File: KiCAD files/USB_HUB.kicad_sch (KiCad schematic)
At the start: 23 parts, among them U1 SL2.1S

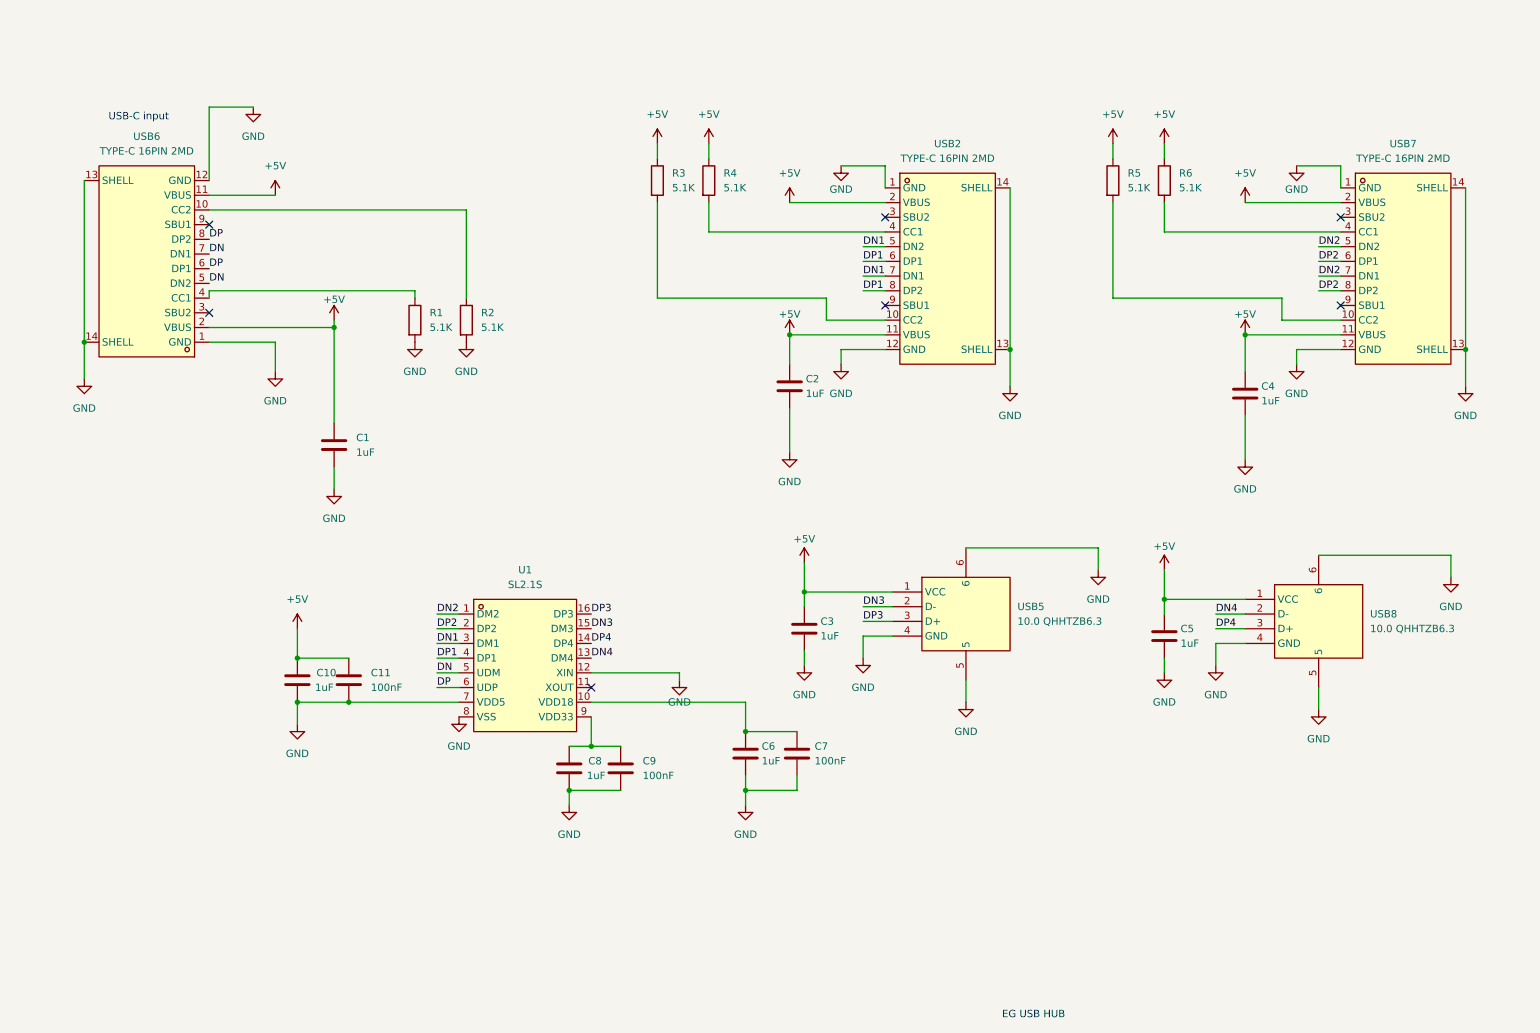
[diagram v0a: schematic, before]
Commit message: Updated board design to include ESD. Not changed: Zine, README except BOM
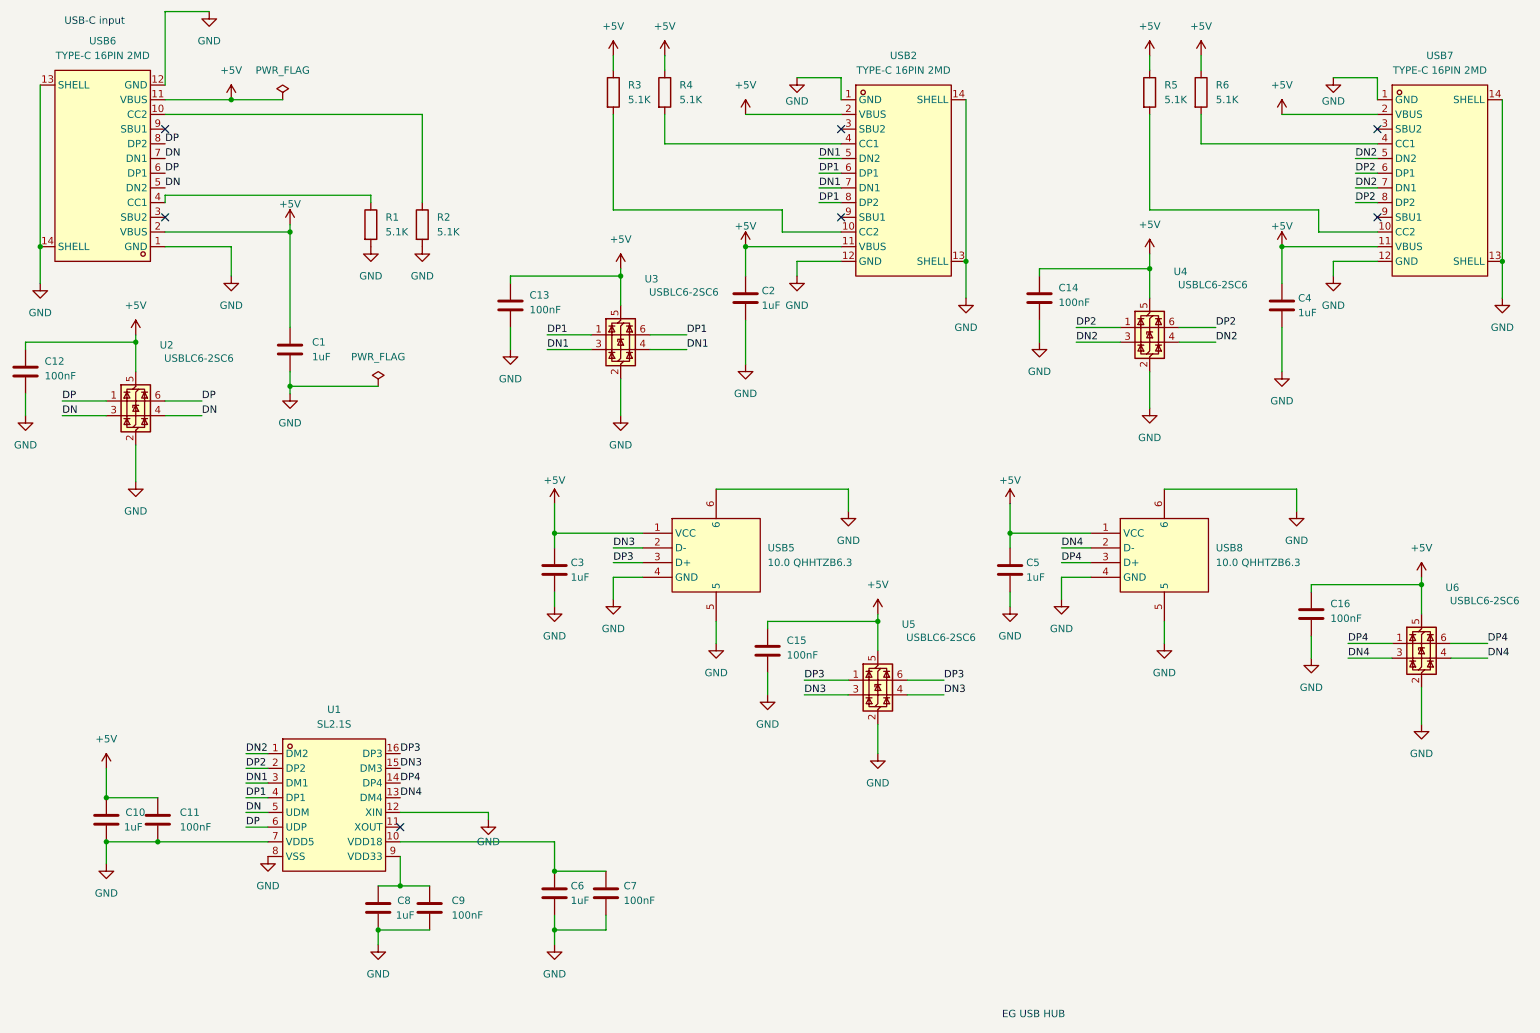
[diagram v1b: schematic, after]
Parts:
- added C12, C13, C14, C15, C16: 100nF, Capacitor_SMD:C_0402_1005Metric, symbol Device:C
- added U2, U3, U4, U5, U6: USBLC6-2SC6, Package_TO_SOT_SMD:SOT-23-6, symbol Power_Protection:USBLC6-2SC6
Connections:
- net +5V: now also C12.1, C13.1, C14.1, C15.1, C16.1, U2.5 (VBUS), U3.5 (VBUS), U4.5 (VBUS), U5.5 (VBUS), U6.5 (VBUS)
- net DN: now also U2.3 (I/O2), U2.4 (I/O2)
- net DN1: now also U3.3 (I/O2), U3.4 (I/O2)
- net DN2: now also U4.3 (I/O2), U4.4 (I/O2)
- net DN3: now also U5.3 (I/O2), U5.4 (I/O2)
- net DN4: now also U6.3 (I/O2), U6.4 (I/O2)
- net DP: now also U2.1 (I/O1), U2.6 (I/O1)
- net DP1: now also U3.1 (I/O1), U3.6 (I/O1)
- net DP2: now also U4.1 (I/O1), U4.6 (I/O1)
- net DP3: now also U5.1 (I/O1), U5.6 (I/O1)
- net DP4: now also U6.1 (I/O1), U6.6 (I/O1)
- net GND: now also C12.2, C13.2, C14.2, C15.2, C16.2, U2.2 (GND), U3.2 (GND), U4.2 (GND), U5.2 (GND), U6.2 (GND)
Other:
- moved on the sheet: C1, C10, C11, C2, C3, C4, C5, C6, C7, C8, C9, R1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
